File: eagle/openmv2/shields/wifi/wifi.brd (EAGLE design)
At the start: 35.6 x 26.7 mm, 20 parts, among them U2 OPENMV3

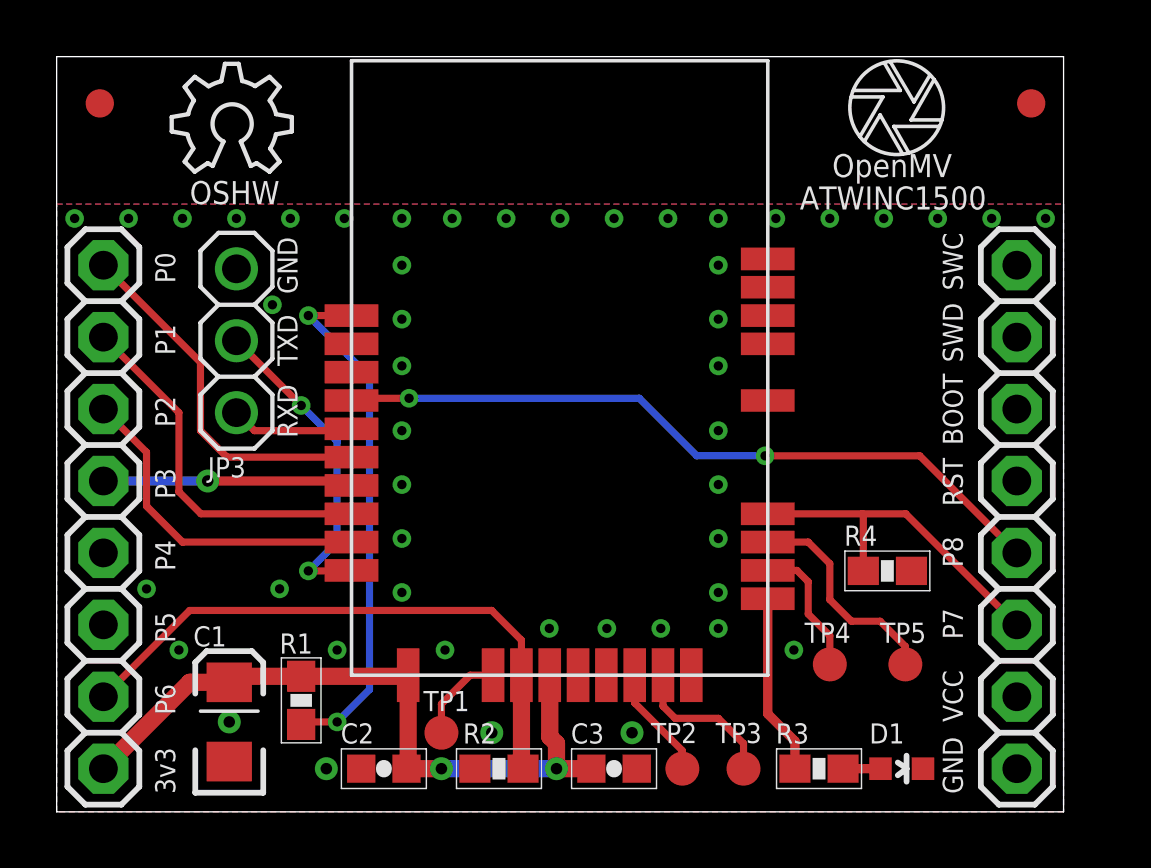
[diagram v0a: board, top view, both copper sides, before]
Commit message: Update shields silk-screen.
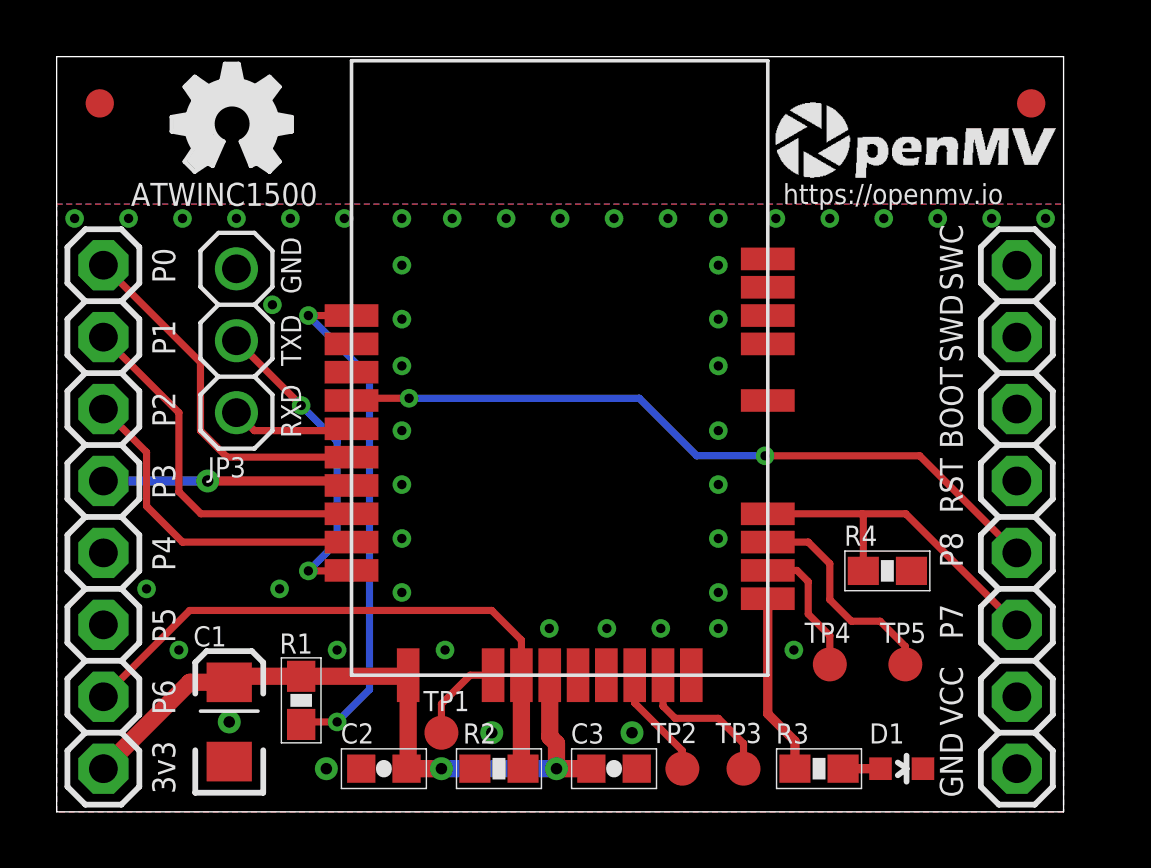
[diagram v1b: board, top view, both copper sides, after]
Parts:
- removed LOGO1: OSHW_LOGO_6MILX0150-NT, iofault:OSHW_6X150_NOTEXT
- added U$10: (no value), openmv:OMV-LOGO-SMALL
- added U$5: (no value), openmv:ROHS
- added U$6: (no value), openmv:WEEE
- added U$7: (no value), iofault:OSHW_FILLX150_NOTEXT
- U$4: value OPENMV-LOGO -> (none); device openmv:OPENMV-LOGO -> openmv:OMV-LOGO
- moved U$4 4.08 mm to (24.0, 22.9), flipped to the bottom
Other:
- board text added: "2/11/2016"
- board text added: "Built by MacroFab"
- board text added: "Made in USA"
- board text added: "WiFi Shield R2"
- board text added: "https://openmv.io"
- board text removed: "0.5 oz copper"
- board text removed: "1 oz copper"
- board text removed: "47 mil core"
- board text removed: "6.7 mil prepreg"
- board text removed: "Antenna trace 12mils (50Ohms impedance)"
- board text removed: "OSHW"
- board text removed: "OpenMV"
- board text removed: "Stackup:"
- board text removed: "er is 3.66"

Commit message: Update WINC1500 to Rev-B
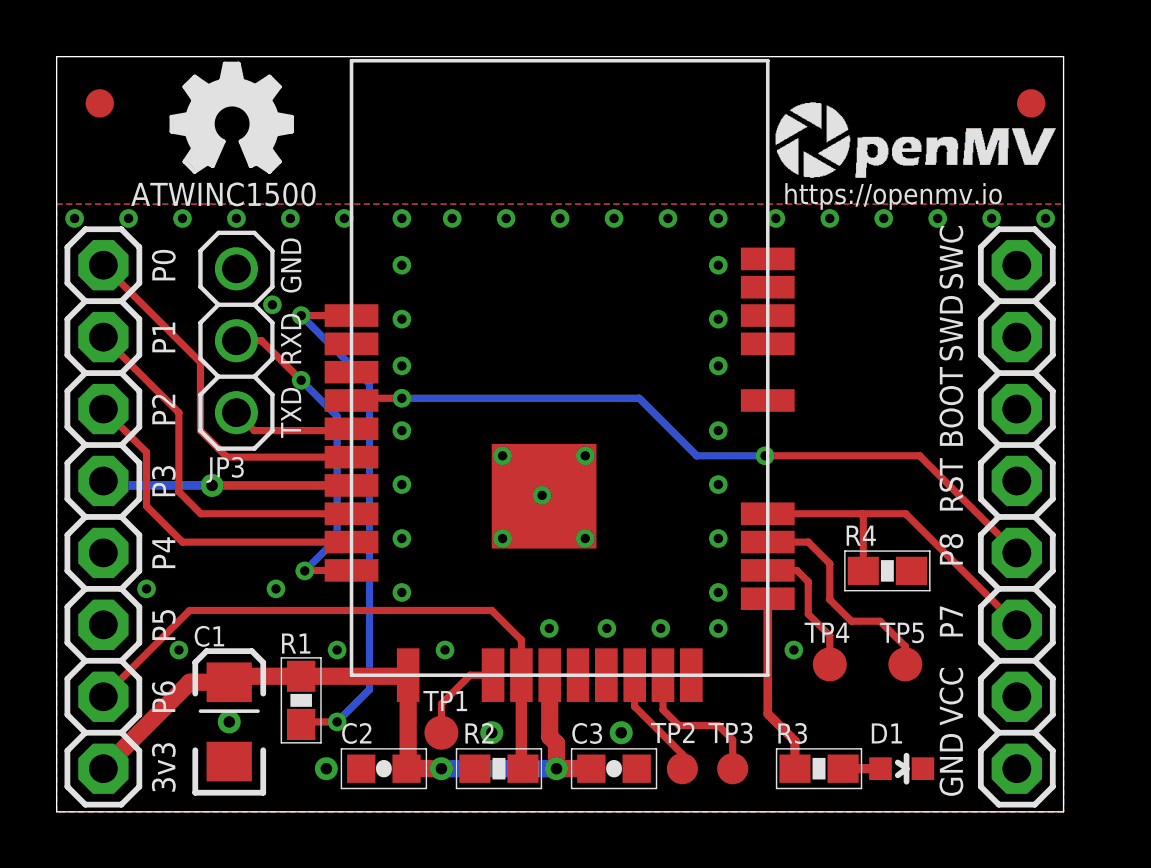
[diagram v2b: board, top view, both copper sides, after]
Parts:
- TP2, TP3: value TPTP12R -> TPTP11R; device testpad:TP12R -> testpad:TP11R
- moved TP3 0.38 mm to (23.9, 1.52)
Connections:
- net GND: now also U$3.P$29
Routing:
- net DBG_RXD: track 11.6 -> 12.3 mm
